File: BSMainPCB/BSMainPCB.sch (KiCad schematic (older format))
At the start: 1006 parts, among them Q1 2N7002, Q10 IRF9321, Q11 2N7002, Q12 IRF9321, Q13 2N7002, Q14 IRF9321, Q15 2N7002, Q16 IRF9321, Q17 2N7002, Q18 IRF9321, Q2 IRF9321, Q3 2N7002, Q4 IRF9321, Q5 2N7002, Q6 IRF9321, Q7 2N7002, Q8 IRF9321, Q9 2N7002, SW1 SWITCH_H, U1 USBLC6

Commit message: Layout started
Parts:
- removed C38: DoNotMount, Capacitors:CAP_0402, symbol Tittar_kl:C
- removed TP31: TESTPOINT, PCB:TESTPOINT_1MM, symbol pcb_details:TESTPOINT
- ANT1: footprint Radio:ANT_868_IFA_SIMPLEJOY -> Antennas:ANT_868_IFA_SIMPLEJOY
- L2: footprint Inductors:IND_SDR0604 -> Inductors:SDR0604
- XL1: footprint Connectors:PLS-6-NoHole -> Connectors:PLS-6_LOCK
- XL4: footprint Connectors:uUSB_614105150721 -> Connectors:USBmicro_MOLEX_1050170001
- XTAL2: footprint Quartz:0503x4-4 -> Quartz:03225C4
- renumbered C101 to C100, C102 to C101, C103 to C102, C104 to C103, C105 to C104, C106 to C105, C107 to C106, C108 to C107, C109 to C108, C110 to C109, C111 to C110, C112 to C111, C113 to C112, C114 to C113, C115 to C114, C116 to C115, C117 to C116, C118 to C117, C119 to C118, C120 to C119, C121 to C120, C122 to C121, C123 to C122, C124 to C123, C125 to C124, C126 to C125, C127 to C126, C128 to C127, C129 to C128, C130 to C129, C131 to C130, C132 to C131, C133 to C132, C134 to C133, C135 to C134, C136 to C135, C137 to C136, C138 to C137, C139 to C138, C140 to C139, C141 to C140, C142 to C141, C143 to C142, C144 to C143, C145 to C144, C146 to C145, C147 to C146, C148 to C147, C149 to C148, C150 to C149, C151 to C150, C152 to C151, C153 to C152, C154 to C153, C155 to C154, C156 to C155, C157 to C156, C158 to C157, C159 to C158, C160 to C159, C161 to C160, C162 to C161, C163 to C162, C164 to C163, C165 to C164, C166 to C165, C167 to C166, C168 to C167, C169 to C168, C170 to C169, C171 to C170, C172 to C171, C173 to C172, C174 to C173, C175 to C174, C176 to C175, C177 to C176, C178 to C177, C179 to C178, C180 to C179, C181 to C180, C182 to C181, C183 to C182, C184 to C183, C185 to C184, C186 to C185, C187 to C186, C188 to C187, C189 to C188, C190 to C189, C191 to C190, C192 to C191, C193 to C192, C194 to C193, C195 to C194, C196 to C195, C197 to C196, C198 to C197, C199 to C198, C200 to C199, C201 to C200, C202 to C201, C203 to C202, C204 to C203, C205 to C204, C206 to C205, C207 to C206, C208 to C207, C209 to C208, C210 to C209, C211 to C210, C212 to C211, C213 to C212, C214 to C213, C215 to C214, C216 to C215, C217 to C216, C218 to C217, C219 to C218, C220 to C219, C221 to C220, C222 to C221, C223 to C222, C224 to C223, C225 to C224, C226 to C225, C227 to C226, C228 to C227, C229 to C228, C230 to C229, C231 to C230, C232 to C231, C233 to C232, C234 to C233, C235 to C234, C236 to C235, C237 to C236, C238 to C237, C239 to C238, C240 to C239, C241 to C240, C242 to C241, C243 to C242, C244 to C243, C245 to C244, C246 to C245, C247 to C246, C248 to C247, C249 to C248, C250 to C249, C251 to C250, C252 to C251, C253 to C252, C254 to C253, C255 to C254, C256 to C255, C257 to C256, C258 to C257, C259 to C258, C260 to C259, C261 to C260, C262 to C261, C263 to C262, C264 to C263, C265 to C264, C266 to C265, C267 to C266, C268 to C267, C269 to C268, C270 to C269, C271 to C270, C272 to C271, C273 to C272, C274 to C273, C275 to C274, C276 to C275, C277 to C276, C278 to C277, C279 to C278, C280 to C279, C281 to C280, C282 to C281, C283 to C282, C284 to C283, C285 to C284, C286 to C285, C287 to C286, C288 to C287, C289 to C288, C290 to C289, C291 to C290, C292 to C291, C293 to C292, C294 to C293, C295 to C294, C296 to C295, C297 to C296, C298 to C297, C299 to C298, C300 to C299, C301 to C300, C302 to C301, C303 to C302, C304 to C303, C305 to C304, C306 to C305, C307 to C306, C308 to C307, C309 to C308, C310 to C309, C311 to C310, C312 to C311, C313 to C312, C314 to C313, C315 to C314, C316 to C315, C317 to C316, C318 to C317, C319 to C318, C320 to C319, C321 to C320, C322 to C321, C323 to C322, C324 to C323, C325 to C324, C326 to C325, C327 to C326, C328 to C327, C329 to C328, C330 to C329, C331 to C330, C332 to C331, C333 to C332, C334 to C333, C335 to C334, C336 to C335, C337 to C336, C338 to C337, C339 to C338, C340 to C339, C341 to C340, C342 to C341, C343 to C342, C344 to C343, C345 to C344, C346 to C345, C347 to C346, C348 to C347, C349 to C348, C350 to C349, C351 to C350, C352 to C351, C353 to C352, C354 to C353, C355 to C354, C356 to C355, C357 to C356, C358 to C357, C359 to C358, C360 to C359, C361 to C360, C362 to C361, C363 to C362, C364 to C363, C39 to C38, C40 to C39, C41 to C40, C42 to C41, C43 to C42, C44 to C43, C45 to C44, C46 to C45, C47 to C46, C48 to C47, C49 to C48, C50 to C49, C51 to C50, C52 to C51, C53 to C52, C54 to C53, C55 to C54, C56 to C55, C57 to C56, C58 to C57, C59 to C58, C60 to C59, C61 to C60, C62 to C61, C63 to C62, C64 to C63, C65 to C64, C66 to C65, C67 to C66, C68 to C67, C69 to C68, C70 to C69, C71 to C70, C72 to C71, C73 to C72, C74 to C73, C75 to C74, C76 to C75, C77 to C76, C78 to C77, C79 to C78, C80 to C79, C81 to C80, C82 to C81, C83 to C82, C84 to C83, C85 to C84, C86 to C85, C87 to C86, C88 to C87, C89 to C88, C90 to C89, C91 to C90, C92 to C91, C93 to C92, C94 to C93, C95 to C94, C96 to C95, C97 to C96, C98 to C97, C99 to C98, C100 to C99, R11 to R10, R12 to R11, R2 to R12, R3 to R2, R4 to R3, R5 to R4, R6 to R5, R7 to R6, R8 to R7, R9 to R8, R10 to R9, TP2 to TP1, TP3 to TP2, TP1 to TP3
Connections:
- net +3v3: now also DD6.16 (VCC)
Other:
- moved on the sheet: R12, TP3

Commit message: - Lot of capacitors near LEDs removed, as eDesignSuite shows they are not required
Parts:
- removed C100, C101, C102, C103, C104, C105, C106, C107, C108, C109, C110, C111, C170, C171, C172, C173, C174, C175, C176, C177, C178, C179, C180, C181, C182, C183, C242, C243, C244, C245, C246, C247, C248, C249, C250, C251, C252, C253, C254, C255, C314, C315, C316, C317, C318, C319, C320, C321, C322, C323, C324, C325, C326, C327, C357, C358, C359, C360, C361, C362, C363, C98, C99: 0.1u, Capacitors:CAP_0603, symbol Tittar_kl:C
- removed C156, C157, C158, C159, C160, C161, C162, C163, C164, C165, C166, C167, C168, C169, C228, C229, C230, C231, C232, C233, C234, C235, C236, C237, C238, C239, C240, C241, C300, C301, C302, C303, C304, C305, C306, C307, C308, C309, C310, C311, C312, C313, C350, C351, C352, C353, C354, C355, C356, C84, C85, C86, C87, C88, C89, C90, C91, C92, C93, C94, C95, C96, C97: 10u, Capacitors:CAP_0805, symbol Tittar_kl:C

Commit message: * Hole connection changed
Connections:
- net GND: no longer HOLE10.H, HOLE11.H, HOLE12.H, HOLE9.H
- net GNDPWR: now also HOLE10.H, HOLE11.H, HOLE12.H, HOLE9.H
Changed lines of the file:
@@
-$EndComp
-$Comp
-L power:GND #PWR0743
-U 1 1 5E17CB9E
-P 32250 21450
-F 0 "#PWR0743" H 32340 21430 30  0001 C CNN
-F 1 "GND" H 32250 21370 30  0001 C CNN
-F 2 "" H 32250 21450 60  0001 C CNN
-F 3 "" H 32250 21450 60  0001 C CNN
-	1    32250 21450
-	1    0    0    -1
 $EndComp
 $Comp
@@
 Wire Wire Line
 	16550 19050 17300 19050
+$Comp
+L power:GNDPWR #PWR?
+U 1 1 5DA1ED95
+P 32250 21450
+F 0 "#PWR?" H 32250 21500 40  0001 C CNN
+F 1 "GNDPWR" H 32250 21370 40  0001 C CNN
+F 2 "" H 32250 21450 60  0000 C CNN
+F 3 "" H 32250 21450 60  0000 C CNN
+	1    32250 21450
+	1    0    0    -1
+$EndComp
 $EndSCHEMATC

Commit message: Proceeding with layout
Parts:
- removed C2, C30: 100u, Capacitors:SMD_D6d3, symbol Tittar_kl:CP
- removed HOLE10, HOLE11, HOLE12, HOLE5, HOLE6, HOLE7, HOLE8, HOLE9: HOLE_METALLED, PCB:Hole3_5_out6mm, symbol pcb_details:HOLE_METALLED
- added C2, C30: 10u, Capacitors:CAP_0805, symbol Tittar_kl:C
- added L68: BLM15AG102, Inductors:IND_0402, symbol Tittar_kl:L
- added Q19: 2N7002, SOT:SOT23-3, symbol Transistors_kl:N_3PIN
- added Q20: IRLML9303, SOT:SOT23-3, symbol Transistors_kl:P_3PIN
- added R262: 100k, Resistors:RES_0603, symbol Tittar_kl:R
- added R263: 1k, Resistors:RES_0603, symbol Tittar_kl:R
- added TP31: TESTPOINT, PCB:TESTPOINT_1MM, symbol pcb_details:TESTPOINT
- added XL79: CONN_2, Connectors:W02_Pitch_2d54, symbol Connectors_kl:CONN_2
- ANT1: footprint Antennas:ANT_868_IFA_SIMPLEJOY -> Antennas:ANT_868_IFA_SIMPLEJOY_MIRR
- C1, C10, C11, C12, C127, C128, C129, C13, C130, C131, C132, C133, C134, C135, C136, C137, C138, C139, C14, C140, C15, C16, C17, C18, C19, C199, C20, C200, C201, C202, C203, C204, C205, C206, C207, C208, C209, C210, C211, C212, C22, C24, C25, C26, C27, C271, C272, C273, C274, C275, C276, C277, C278, C279, C28, C280, C281, C282, C283, C284, C3, C31, C32, C336, C337, C338, C339, C34, C340, C341, C342, C36, C37, C38, C39, C4, C55, C56, C57, C58, C59, C60, C61, C62, C63, C64, C65, C66, C67, C68, C7, C8, C9: footprint Capacitors:CAP_0603 -> Capacitors:CAP_0603_Silks
- C21: value 0.1u -> 1u; footprint Capacitors:CAP_0603 -> Capacitors:CAP_0603_Silks
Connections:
- net +3v3: now also C2.2
- net GND: now also C2.1; no longer C20.2, C23.2, D10.C, D11.C, D3.C, D4.C, D5.C, D6.C, D7.C, D8.C, D9.C, HOLE1.H, HOLE2.H, HOLE3.H
- net GNDPWR: now also C20.2, C23.2, D10.C, D11.C, D3.C, D4.C, D5.C, D6.C, D7.C, D8.C, D9.C, HOLE1.H, HOLE2.H, HOLE3.H, C30.2, Q19.2 (S), R262.1, XL79.1 (P1)
- net LED_PWR8: now also DD2.3 ((OC32IN)/PC14); no longer DD2.2 (PC13)
- net LED_PWR9: now also DD2.4 ((OC32OUT)/PC15); no longer DD2.3 ((OC32IN)/PC14)
- net PWR_CTRL5: now also DD2.40 (MCO2/T8C4/SDA3/T3C4/SDIO_D1/PC9); no longer DD2.39 (T8C3/T3C3/CK6/SDIO_D0/PC8)
- net PWR_CTRL6: now also DD2.51 (SCK3/TX4/TX3/SDIO_D2/PC10); no longer DD2.40 (MCO2/T8C4/SDA3/T3C4/SDIO_D1/PC9)
- net PWR_CTRL7: now also DD2.52 (MISO3/RX4/RX3/SDIO_D3/PC11); no longer DD2.51 (SCK3/TX4/TX3/SDIO_D2/PC10)
- net PWR_CTRL8: now also DD2.53 (MOSI3/TX5/CK3/SDIO_CK/PC12); no longer DD2.52 (MISO3/RX4/RX3/SDIO_D3/PC11)
- net PWR_CTRL9: now also DD2.2 (PC13); no longer DD2.53 (MOSI3/TX5/CK3/SDIO_CK/PC12)
- net PwrMCU: now also L68.2; no longer C21.1, DD2.13 (VDDA)
- net PwrUnst: now also C30.1, Q20.2 (S), R263.1
- new net: C21.1, DD2.13 (VDDA), L68.1
- new net: Q20.3 (D), XL79.2 (PM)
- new net: Q19.3 (D), Q20.1 (G), R263.2
- new net VENT_CTRL: DD2.39 (T8C3/T3C3/CK6/SDIO_D0/PC8), Q19.1 (G), R262.2, TP31.1
- no-connect marks 7 -> 6
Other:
- note added: "Cooler control"
- moved on the sheet: TP24, TP25, TP26, TP27, TP28

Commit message: Proceeding with layout
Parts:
- C112, C141, C184, C213, C23, C256, C285, C335, C40, C69: footprint Capacitors:CAP_10xxR -> Capacitors:CAP_10Rx16_HOR
- XL4: symbol Connectors_kl:USB_MICRO_2H -> Connectors_kl:USB_MICRO_4H
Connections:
- net at C1.2, R1.1, XL4.H1: now also XL4.H2, XL4.H3, XL4.H4
- no-connect marks 6 -> 5
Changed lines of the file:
@@
 	6550 2350 7000 2350
 Wire Wire Line
-	800  14050 1100 14050
+	800  14050 900  14050
 Wire Wire Line
 	2300 3150 2450 3150
@@
 $EndComp
 $Comp
-L Connectors_kl:USB_MICRO_2H XL4
+L Connectors_kl:USB_MICRO_4H XL4
 U 1 1 5D6B429E
 P 1150 13450
@@
 Connection ~ 1400 13050
 Connection ~ 1400 13650
-NoConn ~ 900  13950
 Connection ~ 1800 4300
 NoConn ~ 4150 13400
@@
 F 0 "C23" H 3000 21650 50  0000 L CNN
 F 1 "1000u" H 3000 21450 50  0000 L CNN
-F 2 "Capacitors:CAP_10xxR" H 2950 21550 60  0001 C CNN
+F 2 "Capacitors:CAP_10Rx16_HOR" H 2950 21550 60  0001 C CNN
 F 3 "" H 2950 21550 60  0000 C CNN
 F 4 "JRB1E102M05001000210000B " H 2950 21550 50  0001 C CNN "PN"
@@
 F 0 "C40" H 7800 21800 50  0000 L CNN
 F 1 "1000u" H 7800 21600 50  0000 L CNN
-F 2 "Capacitors:CAP_10xxR" H 7750 21700 60  0001 C CNN
+F 2 "Capacitors:CAP_10Rx16_HOR" H 7750 21700 60  0001 C CNN
 F 3 "" H 7750 21700 60  0000 C CNN
 F 4 "JRB1E102M05001000210000B " H 7750 21700 50  0001 C CNN "PN"
@@
 F 0 "C69" H 10200 21800 50  0000 L CNN
 F 1 "1000u" H 10200 21600 50  0000 L CNN
-F 2 "Capacitors:CAP_10xxR" H 10150 21700 60  0001 C CNN
+F 2 "Capacitors:CAP_10Rx16_HOR" H 10150 21700 60  0001 C CNN
 F 3 "" H 10150 21700 60  0000 C CNN
 F 4 "JRB1E102M05001000210000B " H 10150 21700 50  0001 C CNN "PN"
@@
 F 0 "C112" H 12600 21800 50  0000 L CNN
 F 1 "1000u" H 12600 21600 50  0000 L CNN
-F 2 "Capacitors:CAP_10xxR" H 12550 21700 60  0001 C CNN
+F 2 "Capacitors:CAP_10Rx16_HOR" H 12550 21700 60  0001 C CNN
 F 3 "" H 12550 21700 60  0000 C CNN
 F 4 "JRB1E102M05001000210000B " H 12550 21700 50  0001 C CNN "PN"
@@
 F 0 "C141" H 15050 21800 50  0000 L CNN
 F 1 "1000u" H 15050 21600 50  0000 L CNN
-F 2 "Capacitors:CAP_10xxR" H 15000 21700 60  0001 C CNN
+F 2 "Capacitors:CAP_10Rx16_HOR" H 15000 21700 60  0001 C CNN
 F 3 "" H 15000 21700 60  0000 C CNN
 F 4 "JRB1E102M05001000210000B " H 15000 21700 50  0001 C CNN "PN"
@@
 F 0 "C184" H 17500 21800 50  0000 L CNN
 F 1 "1000u" H 17500 21600 50  0000 L CNN
-F 2 "Capacitors:CAP_10xxR" H 17450 21700 60  0001 C CNN
+F 2 "Capacitors:CAP_10Rx16_HOR" H 17450 21700 60  0001 C CNN
 F 3 "" H 17450 21700 60  0000 C CNN
 F 4 "JRB1E102M05001000210000B " H 17450 21700 50  0001 C CNN "PN"
@@
 F 0 "C213" H 20150 21800 50  0000 L CNN
 F 1 "1000u" H 20150 21600 50  0000 L CNN
-F 2 "Capacitors:CAP_10xxR" H 20100 21700 60  0001 C CNN
+F 2 "Capacitors:CAP_10Rx16_HOR" H 20100 21700 60  0001 C CNN
 F 3 "" H 20100 21700 60  0000 C CNN
 F 4 "JRB1E102M05001000210000B " H 20100 21700 50  0001 C CNN "PN"
@@
 F 0 "C256" H 22600 21800 50  0000 L CNN
 F 1 "1000u" H 22600 21600 50  0000 L CNN
-F 2 "Capacitors:CAP_10xxR" H 22550 21700 60  0001 C CNN
+F 2 "Capacitors:CAP_10Rx16_HOR" H 22550 21700 60  0001 C CNN
 F 3 "" H 22550 21700 60  0000 C CNN
 F 4 "JRB1E102M05001000210000B " H 22550 21700 50  0001 C CNN "PN"
@@
 F 0 "C285" H 25250 21800 50  0000 L CNN
 F 1 "1000u" H 25250 21600 50  0000 L CNN
-F 2 "Capacitors:CAP_10xxR" H 25200 21700 60  0001 C CNN
+F 2 "Capacitors:CAP_10Rx16_HOR" H 25200 21700 60  0001 C CNN
 F 3 "" H 25200 21700 60  0000 C CNN
 F 4 "JRB1E102M05001000210000B " H 25200 21700 50  0001 C CNN "PN"
@@
 F 0 "C335" H 27750 21850 50  0000 L CNN
 F 1 "1000u" H 27750 21650 50  0000 L CNN
-F 2 "Capacitors:CAP_10xxR" H 27700 21750 60  0001 C CNN
+F 2 "Capacitors:CAP_10Rx16_HOR" H 27700 21750 60  0001 C CNN
 F 3 "" H 27700 21750 60  0000 C CNN
 F 4 "JRB1E102M05001000210000B " H 27700 21750 50  0001 C CNN "PN"
@@
 Text Notes 30350 14600 0    50   ~ 0
 Cooler control
+Wire Wire Line
+	900  13950 900  14050
+Connection ~ 900  14050
+Wire Wire Line
+	900  14050 1000 14050
+Wire Wire Line
+	1000 13950 1000 14050
+Connection ~ 1000 14050
+Wire Wire Line
+	1000 14050 1100 14050
+Wire Wire Line
+	1100 13950 1100 14050
+Connection ~ 1100 14050
 $EndSCHEMATC

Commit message: + Tracing done
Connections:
- net PWR_IN2: now reaches Q4.1 (S), Q4.2 (S), Q4.3 (S), R22.1, TP95.1, XL7.1 (P1)
- net PWR_IN3: now reaches Q6.1 (S), Q6.2 (S), Q6.3 (S), R56.1, TP97.1, XL8.1 (P1)
- net PWR_IN4: now reaches Q8.1 (S), Q8.2 (S), Q8.3 (S), R72.1, TP99.1, XL23.1 (P1)
- net PWR_IN5: now reaches Q10.1 (S), Q10.2 (S), Q10.3 (S), R120.1, TP101.1, XL24.1 (P1)
- net PWR_IN6: now reaches Q12.1 (S), Q12.2 (S), Q12.3 (S), R122.1, TP103.1, XL39.1 (P1)
- net PWR_IN7: now reaches Q14.1 (S), Q14.2 (S), Q14.3 (S), R170.1, TP105.1, XL40.1 (P1)
- net PWR_IN8: now reaches Q16.1 (S), Q16.2 (S), Q16.3 (S), R186.1, TP107.1, XL55.1 (P1)
- net PWR_IN9: now reaches Q18.1 (S), Q18.2 (S), Q18.3 (S), R220.1, TP109.1, XL56.1 (P1)
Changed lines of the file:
@@
 $EndComp
 $Comp
-L Tittar_kl:L L18
-U 1 1 5DD60954
-P 11550 19050
-F 0 "L18" V 11650 19000 40  0000 C CNN
-F 1 "2.2uH" V 11500 19050 40  0000 C CNN
-F 2 "Inductors:IND_SRN2512" V 11610 19060 40  0001 C CNN
-F 3 "" V 11450 18910 60  0001 C CNN
-F 4 "7" V 11550 19010 60  0001 C CNN "Price"
-F 5 "2" V 11650 19110 60  0001 C CNN "SolderPoints"
-F 6 "SRN2512-2R2M" V 11550 19050 60  0001 C CNN "PN"
-	1    11550 19050
-	0    1    -1   0
-$EndComp
-$Comp
 L Tittar_kl:R R36
 U 1 1 5DD60968
@@
 $EndComp
 $Comp
-L Transistors_kl:P_8PIN Q16
-U 1 1 5E04B5F8
-P 24550 21250
-F 0 "Q16" V 24750 21200 60  0000 L CNN
-F 1 "IRF9321" V 24300 21150 60  0000 L CNN
-F 2 "SO_DIL_TSSOP:SO8HEATSINK" H 24750 21300 60  0001 C CNN
-F 3 "" H 24550 21250 60  0000 C CNN
-F 4 "8" H 24950 21500 60  0001 C CNN "SolderPoints"
-F 5 "27" V 24550 21250 50  0001 C CNN "Price"
-F 6 "IRF9321TRPBF " V 24550 21250 50  0001 C CNN "PN"
-F 7 "https://www.terraelectronica.ru/product/604773" V 24550 21250 50  0001 C CNN "URL"
-	1    24550 21250
-	0    1    -1   0
-$EndComp
-$Comp
 L Tittar_kl:CP C285
 U 1 1 5E04B61F
@@
 	1100 13950 1100 14050
 Connection ~ 1100 14050
+$Comp
+L Transistors_kl:P_8PIN Q16
+U 1 1 5E04B5F8
+P 24550 21250
+F 0 "Q16" V 24750 21200 60  0000 L CNN
+F 1 "IRF9321" V 24300 21150 60  0000 L CNN
+F 2 "SO_DIL_TSSOP:SO8HEATSINK" H 24750 21300 60  0001 C CNN
+F 3 "" H 24550 21250 60  0000 C CNN
+F 4 "8" H 24950 21500 60  0001 C CNN "SolderPoints"
+F 5 "27" V 24550 21250 50  0001 C CNN "Price"
+F 6 "IRF9321TRPBF " V 24550 21250 50  0001 C CNN "PN"
+F 7 "https://www.terraelectronica.ru/product/604773" V 24550 21250 50  0001 C CNN "URL"
+	1    24550 21250
+	0    1    -1   0
+$EndComp
+$Comp
+L Tittar_kl:L L18
+U 1 1 5DD60954
+P 11550 19050
+F 0 "L18" V 11650 19000 40  0000 C CNN
+F 1 "2.2uH" V 11500 19050 40  0000 C CNN
+F 2 "Inductors:IND_SRN2512" V 11610 19060 40  0001 C CNN
+F 3 "" V 11450 18910 60  0001 C CNN
+F 4 "7" V 11550 19010 60  0001 C CNN "Price"
+F 5 "2" V 11650 19110 60  0001 C CNN "SolderPoints"
+F 6 "SRN2512-2R2M" V 11550 19050 60  0001 C CNN "PN"
+	1    11550 19050
+	0    1    -1   0
+$EndComp
+Text Label 9000 21000 0    50   ~ 0
+PWR_IN2
+Text Label 11450 21000 0    50   ~ 0
+PWR_IN3
+Text Label 13850 21000 0    50   ~ 0
+PWR_IN4
+Text Label 16350 21000 0    50   ~ 0
+PWR_IN5
+Text Label 19000 21000 0    50   ~ 0
+PWR_IN6
+Text Label 21450 21000 0    50   ~ 0
+PWR_IN7
+Text Label 24100 21000 0    50   ~ 0
+PWR_IN8
+Text Label 26600 21050 0    50   ~ 0
+PWR_IN9
 $EndSCHEMATC

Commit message: PCB sent to factory
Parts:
- Logo1: footprint Pictures:Ostranna_12d7_10d1 -> Pictures:Ostranna_16d9_13d5
- Q10, Q12, Q14, Q16, Q18, Q2, Q4, Q6, Q8: symbol Transistors_kl:P_8PIN -> Transistors_kl:P_8PIN_W_PAD
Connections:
- net GNDPWR: now also Q10.PAD, Q12.PAD, Q14.PAD, Q16.PAD, Q18.PAD, Q2.PAD, Q4.PAD, Q6.PAD, Q8.PAD
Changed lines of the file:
@@
 F 0 "Logo1" H 28850 21650 60  0000 L CNN
 F 1 "Logo" H 28850 21550 60  0000 L CNN
-F 2 "Pictures:Ostranna_12d7_10d1" H 28950 21100 60  0001 C CNN
+F 2 "Pictures:Ostranna_16d9_13d5" H 28950 21100 60  0001 C CNN
 F 3 "" H 28950 21100 60  0000 C CNN
 F 4 "0" H 28950 21100 60  0001 C CNN "SolderPoints"
@@
 $EndComp
 $Comp
-L Transistors_kl:P_8PIN Q2
+L Transistors_kl:P_8PIN_W_PAD Q2
 U 1 1 5C956171
 P 7100 21250
@@
 	7550 20950 7550 21000
 $Comp
-L Transistors_kl:P_8PIN Q4
+L Transistors_kl:P_8PIN_W_PAD Q4
 U 1 1 5E032CC7
 P 9500 21250
@@
 Connection ~ 9150 21000
 $Comp
-L Transistors_kl:P_8PIN Q6
+L Transistors_kl:P_8PIN_W_PAD Q6
 U 1 1 5E03C997
 P 11900 21250
@@
 $EndComp
 $Comp
-L Transistors_kl:P_8PIN Q8
+L Transistors_kl:P_8PIN_W_PAD Q8
 U 1 1 5E03CA84
 P 14350 21250
@@
 Connection ~ 11550 21000
 $Comp
-L Transistors_kl:P_8PIN Q10
+L Transistors_kl:P_8PIN_W_PAD Q10
 U 1 1 5E04B2D8
 P 16800 21250
@@
 $EndComp
 $Comp
-L Transistors_kl:P_8PIN Q12
+L Transistors_kl:P_8PIN_W_PAD Q12
 U 1 1 5E04B3C5
 P 19450 21250
@@
 $EndComp
 $Comp
-L Transistors_kl:P_8PIN Q14
+L Transistors_kl:P_8PIN_W_PAD Q14
 U 1 1 5E04B42C
 P 21900 21250
@@
 $EndComp
 $Comp
-L Transistors_kl:P_8PIN Q18
+L Transistors_kl:P_8PIN_W_PAD Q18
 U 1 1 5E08273A
 P 27050 21300
@@
 Connection ~ 1100 14050
 $Comp
-L Transistors_kl:P_8PIN Q16
+L Transistors_kl:P_8PIN_W_PAD Q16
 U 1 1 5E04B5F8
 P 24550 21250
@@
 Text Label 26600 21050 0    50   ~ 0
 PWR_IN9
+Wire Wire Line
+	7200 21650 7200 21500
+$Comp
+L power:GNDPWR #PWR?
+U 1 1 5DA31B72
+P 7200 21650
+F 0 "#PWR?" H 7200 21700 40  0001 C CNN
+F 1 "GNDPWR" H 7200 21570 40  0001 C CNN
+F 2 "" H 7200 21650 60  0000 C CNN
+F 3 "" H 7200 21650 60  0000 C CNN
+	1    7200 21650
+	1    0    0    -1
+$EndComp
+$Comp
+L power:GNDPWR #PWR?
+U 1 1 5DA31B72
+P 9600 21650
+F 0 "#PWR?" H 9600 21700 40  0001 C CNN
+F 1 "GNDPWR" H 9600 21570 40  0001 C CNN
+F 2 "" H 9600 21650 60  0000 C CNN
+F 3 "" H 9600 21650 60  0000 C CNN
+	1    9600 21650
+	1    0    0    -1
+$EndComp
+Wire Wire Line
+	9600 21650 9600 21500
+$Comp
+L power:GNDPWR #PWR?
+U 1 1 5DA613B5
+P 12000 21650
+F 0 "#PWR?" H 12000 21700 40  0001 C CNN
+F 1 "GNDPWR" H 12000 21570 40  0001 C CNN
+F 2 "" H 12000 21650 60  0000 C CNN
+F 3 "" H 12000 21650 60  0000 C CNN
+	1    12000 21650
+	1    0    0    -1
+$EndComp
+Wire Wire Line
+	12000 21650 12000 21500
+$Comp
+L power:GNDPWR #PWR?
+U 1 1 5DA6184A
+P 14450 21650
+F 0 "#PWR?" H 14450 21700 40  0001 C CNN
+F 1 "GNDPWR" H 14450 21570 40  0001 C CNN
+F 2 "" H 14450 21650 60  0000 C CNN
+F 3 "" H 14450 21650 60  0000 C CNN
+	1    14450 21650
+	1    0    0    -1
+$EndComp
+Wire Wire Line
+	14450 21650 14450 21500
+$Comp
+L power:GNDPWR #PWR?
+U 1 1 5DA61F8B
+P 16900 21650
+F 0 "#PWR?" H 16900 21700 40  0001 C CNN
+F 1 "GNDPWR" H 16900 21570 40  0001 C CNN
+F 2 "" H 16900 21650 60  0000 C CNN
+F 3 "" H 16900 21650 60  0000 C CNN
+	1    16900 21650
+	1    0    0    -1
+$EndComp
+Wire Wire Line
+	16900 21650 16900 21500
+$Comp
+L power:GNDPWR #PWR?
+U 1 1 5DA6251F
+P 19550 21650
+F 0 "#PWR?" H 19550 21700 40  0001 C CNN
+F 1 "GNDPWR" H 19550 21570 40  0001 C CNN
+F 2 "" H 19550 21650 60  0000 C CNN
+F 3 "" H 19550 21650 60  0000 C CNN
+	1    19550 21650
+	1    0    0    -1
+$EndComp
+Wire Wire Line
+	19550 21650 19550 21500
+$Comp
+L power:GNDPWR #PWR?
+U 1 1 5DA62CA2
+P 22000 21650
+F 0 "#PWR?" H 22000 21700 40  0001 C CNN
+F 1 "GNDPWR" H 22000 21570 40  0001 C CNN
+F 2 "" H 22000 21650 60  0000 C CNN
+F 3 "" H 22000 21650 60  0000 C CNN
+	1    22000 21650
+	1    0    0    -1
+$EndComp
+Wire Wire Line
+	22000 21650 22000 21500
+$Comp
+L power:GNDPWR #PWR?
+U 1 1 5DA630EC
+P 24650 21650
+F 0 "#PWR?" H 24650 21700 40  0001 C CNN
+F 1 "GNDPWR" H 24650 21570 40  0001 C CNN
+F 2 "" H 24650 21650 60  0000 C CNN
+F 3 "" H 24650 21650 60  0000 C CNN
+	1    24650 21650
+	1    0    0    -1
+$EndComp
+Wire Wire Line
+	24650 21650 24650 21500
+$Comp
+L power:GNDPWR #PWR?
+U 1 1 5DA639B9
+P 27150 21700
+F 0 "#PWR?" H 27150 21750 40  0001 C CNN
+F 1 "GNDPWR" H 27150 21620 40  0001 C CNN
+F 2 "" H 27150 21700 60  0000 C CNN
+F 3 "" H 27150 21700 60  0000 C CNN
+	1    27150 21700
+	1    0    0    -1
+$EndComp
+Wire Wire Line
+	27150 21700 27150 21550
 $EndSCHEMATC

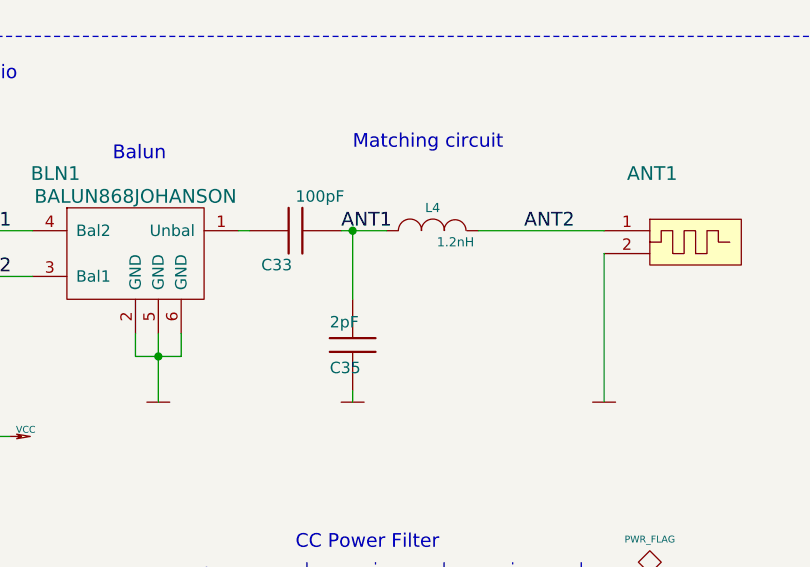
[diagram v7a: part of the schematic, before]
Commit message: + Antenna matched
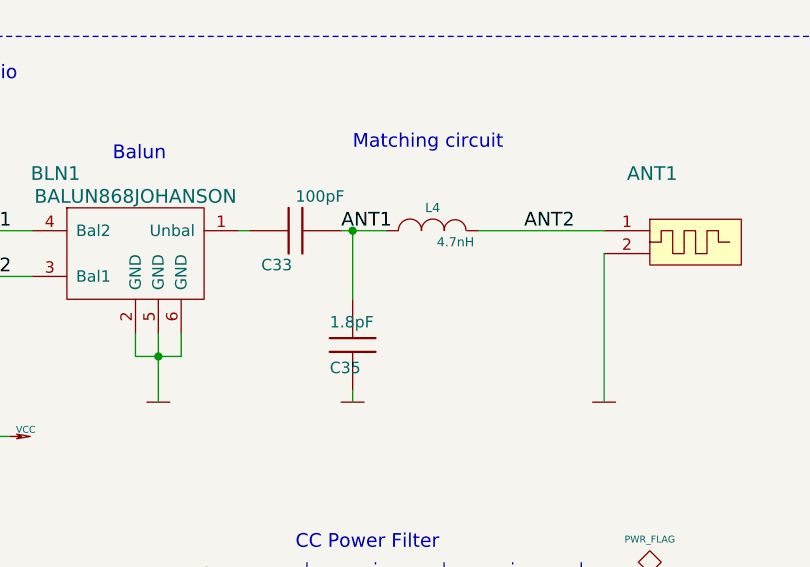
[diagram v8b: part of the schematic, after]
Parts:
- C35: value 2pF -> 1.8pF
- L4: value 1.2nH -> 4.7nH
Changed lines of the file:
@@
 P 6000 6100
 F 0 "L4" V 6100 6100 40  0000 C CNN
-F 1 "1.2nH" V 5950 6200 40  0000 C CNN
+F 1 "4.7nH" V 5950 6200 40  0000 C CNN
 F 2 "Inductors:IND_0402" V 6060 6110 40  0001 C CNN
 F 3 "" V 5900 5960 60  0001 C CNN
@@
 P 5650 6600
 F 0 "C35" H 5550 6500 50  0000 L CNN
-F 1 "2pF" H 5550 6700 50  0000 L CNN
+F 1 "1.8pF" H 5550 6700 50  0000 L CNN
 F 2 "Capacitors:CAP_0402" V 5750 6450 28  0001 C BNN
 F 3 "" H 5550 6500 60  0001 C CNN
